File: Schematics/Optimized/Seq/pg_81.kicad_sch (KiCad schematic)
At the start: 23 parts, among them U8201 F04, U8203 8051, U8204 F04, U8205 F174, U8206 F245, U8207 F240, U8208 F174, U8209 F175, U8210 F194, U8211 F04, U8212 F30, U8213 F04, U8214 F00, U8215 F00, U8216 F38, U8217 F04, U8218 F02, U8219 F00, U8220 F00, U8221 F00, U8222 F00

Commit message: SEQ condensation
Tested: passed run_udiag
Tested: passed expmon_test_seq --quick
Tested: 16.7s (&c) boot_env
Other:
- moved on the sheet: GB244, U8201
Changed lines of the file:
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@@
     (comment 4 "RELEASED")
   )
-  (junction (at 45.72 20.32) (diameter 0) (color 0 0 0 0)
+  (junction (at 142.24 60.96) (diameter 0) (color 0 0 0 0)
   )
   (junction (at 281.94 73.66) (diameter 0) (color 0 0 0 0)
   )
+  (junction (at 208.28 73.66) (diameter 0) (color 0 0 0 0)
+  )
   (junction (at 408.94 243.84) (diameter 0) (color 0 0 0 0)
   )
@@
   )
   (junction (at 40.64 299.72) (diameter 0) (color 0 0 0 0)
-  )
-  (junction (at 213.36 73.66) (diameter 0) (color 0 0 0 0)
   )
   (no_connect (at 515.62 195.58))
@@
     (stroke (width 0) (type default))
   )
-  (wire (pts (xy 40.64 20.32) (xy 45.72 20.32))
+  (wire (pts (xy 137.16 60.96) (xy 142.24 60.96))
     (stroke (width 0) (type default))
   )
@@
     (stroke (width 0) (type default))
   )
-  (wire (pts (xy 96.52 20.32) (xy 213.36 20.32))
+  (wire (pts (xy 193.04 60.96) (xy 208.28 60.96))
     (stroke (width 0) (type default))
   )
@@
     (stroke (width 0) (type default))
   )
-  (wire (pts (xy 157.48 101.6) (xy 177.8 101.6))
+  (wire (pts (xy 172.72 101.6) (xy 177.8 101.6))
     (stroke (width 0) (type default))
   )
@@
     (stroke (width 0) (type default))
   )
-  (wire (pts (xy 175.26 76.2) (xy 190.5 76.2))
+  (wire (pts (xy 182.88 76.2) (xy 190.5 76.2))
     (stroke (width 0) (type default))
   )
@@
     (stroke (width 0) (type default))
   )
-  (wire (pts (xy 213.36 20.32) (xy 213.36 73.66))
+  (wire (pts (xy 208.28 60.96) (xy 208.28 73.66))
     (stroke (width 0) (type default))
   )
@@
     (stroke (width 0) (type default))
   )
+  (wire (pts (xy 208.28 73.66) (xy 236.22 73.66))
+    (stroke (width 0) (type default))
+  )
   (wire (pts (xy 548.64 180.34) (xy 551.18 180.34))
     (stroke (width 0) (type default))
@@
     (stroke (width 0) (type default))
   )
-  (wire (pts (xy 43.18 27.94) (xy 45.72 27.94))
+  (wire (pts (xy 139.7 68.58) (xy 142.24 68.58))
     (stroke (width 0) (type default))
   )
@@
     (stroke (width 0) (type default))
   )
-  (wire (pts (xy 45.72 20.32) (xy 76.2 20.32))
+  (wire (pts (xy 142.24 60.96) (xy 172.72 60.96))
     (stroke (width 0) (type default))
   )
@@
     (stroke (width 0) (type default))
   )
-  (wire (pts (xy 154.94 172.72) (xy 177.8 172.72))
+  (wire (pts (xy 172.72 172.72) (xy 177.8 172.72))
     (stroke (width 0) (type default))
   )
@@
     (stroke (width 0) (type default))
   )
-  (wire (pts (xy 45.72 27.94) (xy 45.72 20.32))
-    (stroke (width 0) (type default))
-  )
-  (wire (pts (xy 213.36 73.66) (xy 236.22 73.66))
+  (wire (pts (xy 142.24 68.58) (xy 142.24 60.96))
     (stroke (width 0) (type default))
   )
@@
     (stroke (width 0) (type default))
   )
-  (wire (pts (xy 142.24 203.2) (xy 177.8 203.2))
+  (wire (pts (xy 162.56 203.2) (xy 177.8 203.2))
     (stroke (width 0) (type default))
   )
@@
     (stroke (width 0) (type default))
   )
-  (wire (pts (xy 175.26 78.74) (xy 175.26 76.2))
+  (wire (pts (xy 182.88 78.74) (xy 182.88 76.2))
     (stroke (width 0) (type default))
   )
@@
     (stroke (width 0) (type default))
   )
-  (wire (pts (xy 215.9 246.38) (xy 241.3 246.38))
+  (wire (pts (xy 215.9 246.38) (xy 223.52 246.38))
     (stroke (width 0) (type default))
   )
@@
     (stroke (width 0) (type default))
   )
-  (wire (pts (xy 208.28 73.66) (xy 213.36 73.66))
-    (stroke (width 0) (type default))
-  )
   (wire (pts (xy 360.68 111.76) (xy 370.84 111.76))
     (stroke (width 0) (type default))
@@
     (effects (font (size 2.54 2.54)) (justify left bottom))
   )
-  (label "WR~" (at 152.4 203.2 0) (fields_autoplaced)
+  (label "WR~" (at 162.56 203.2 0) (fields_autoplaced)
     (effects (font (size 2.54 2.54)) (justify left bottom))
   )
@@
     )
   )
-  (global_label "Q.DIAG_FREEZE~" (shape bidirectional) (at 241.3 246.38 0) (fields_autoplaced)
+  (global_label "Q.DIAG_FREEZE~" (shape bidirectional) (at 223.52 246.38 0) (fields_autoplaced)
     (effects (font (size 2.54 2.54)) (justify left))
-    (property "Intersheetrefs" "${INTERSHEET_REFS}" (at 276.2431 246.2213 0)
+    (property "Intersheetrefs" "${INTERSHEET_REFS}" (at 258.4631 246.2213 0)
       (effects (font (size 1.905 1.905)) (justify left))
     )
@@
     )
   )
-  (global_label "CLK.2X" (shape input) (at 157.48 101.6 180) (fields_autoplaced)
-    (effects (font (size 2.54 2.54)) (justify right))
-    (property "Intersheetrefs" "${INTERSHEET_REFS}" (at 138.6129 101.6 0)
+  (global_label "CLK.2X" (shape input) (at 172.72 101.6 180) (fields_autoplaced)
+    (effects (font (size 2.54 2.54)) (justify right))
+    (property "Intersheetrefs" "${INTERSHEET_REFS}" (at 153.8529 101.6 0)
       (effects (font (size 1.27 1.27)) (justify right))
     )
@@
     )
   )
-  (global_label "FSM_DONE~" (shape input) (at 154.94 172.72 180) (fields_autoplaced)
-    (effects (font (size 2.54 2.54)) (justify right))
-    (property "Intersheetrefs" "${INTERSHEET_REFS}" (at 128.7054 172.5613 0)
+  (global_label "FSM_DONE~" (shape input) (at 172.72 172.72 180) (fields_autoplaced)
+    (effects (font (size 2.54 2.54)) (justify right))
+    (property "Intersheetrefs" "${INTERSHEET_REFS}" (at 146.4854 172.5613 0)
       (effects (font (size 1.905 1.905)) (justify right))
     )
@@
     )
   )
-  (global_label "Q.RESET~" (shape bidirectional) (at 40.64 20.32 180) (fields_autoplaced)
-    (effects (font (size 2.54 2.54)) (justify right))
-    (property "Intersheetrefs" "${INTERSHEET_REFS}" (at 18.6388 20.1613 0)
+  (global_label "Q.RESET~" (shape bidirectional) (at 137.16 60.96 180) (fields_autoplaced)
+    (effects (font (size 2.54 2.54)) (justify right))
+    (property "Intersheetrefs" "${INTERSHEET_REFS}" (at 115.1588 60.8013 0)
       (effects (font (size 1.905 1.905)) (justify right))
     )
@@
     )
   )
-  (symbol (lib_id "r1000:PD") (at 175.26 78.74 0) (unit 1)
+  (symbol (lib_id "r1000:PD") (at 182.88 78.74 0) (unit 1)
     (in_bom no) (on_board yes) (dnp no)
-    (property "Reference" "#PWR0102" (at 175.26 78.74 0)
-      (effects (font (size 1.27 1.27)) hide)
-    )
-    (property "Value" "PD" (at 175.26 78.74 0)
-      (effects (font (size 1.27 1.27)) hide)
-    )
-    (property "Footprint" "" (at 175.26 78.74 0)
-      (effects (font (size 1.27 1.27)) hide)
-    )
-    (property "Datasheet" "" (at 175.26 78.74 0)
+    (property "Reference" "#PWR0102" (at 182.88 78.74 0)
+      (effects (font (size 1.27 1.27)) hide)
+    )
+    (property "Value" "PD" (at 182.88 78.74 0)
+      (effects (font (size 1.27 1.27)) hide)
+    )
+    (property "Footprint" "" (at 182.88 78.74 0)
+      (effects (font (size 1.27 1.27)) hide)
+    )
+    (property "Datasheet" "" (at 182.88 78.74 0)
       (effects (font (size 1.27 1.27)) hide)
     )
@@
     )
   )
-  (symbol (lib_id "r1000:GB") (at 43.18 27.94 0) (mirror y) (unit 1)
+  (symbol (lib_id "r1000:GB") (at 139.7 68.58 0) (mirror y) (unit 1)
     (in_bom yes) (on_board yes) (dnp no)
-    (property "Reference" "GB244" (at 39.37 27.94 0)
-      (effects (font (size 2.54 2.54)) (justify left))
-    )
-    (property "Value" "GB" (at 43.18 27.94 0)
-      (effects (font (size 1.27 1.27)) hide)
-    )
-    (property "Footprint" "" (at 43.18 27.94 0)
-      (effects (font (size 1.27 1.27)) hide)
-    )
-    (property "Datasheet" "" (at 43.18 27.94 0)
+    (property "Reference" "GB244" (at 135.89 68.58 0)
+      (effects (font (size 2.54 2.54)) (justify left))
+    )
+    (property "Value" "GB" (at 139.7 68.58 0)
+      (effects (font (size 1.27 1.27)) hide)
+    )
+    (property "Footprint" "" (at 139.7 68.58 0)
+      (effects (font (size 1.27 1.27)) hide)
+    )
+    (property "Datasheet" "" (at 139.7 68.58 0)
       (effects (font (size 1.27 1.27)) hide)
     )
@@
     )
   )
-  (symbol (lib_id "r1000:F04") (at 86.36 20.32 0) (unit 1)
+  (symbol (lib_id "r1000:F04") (at 182.88 60.96 0) (unit 1)
     (in_bom yes) (on_board yes) (dnp no)
-    (property "Reference" "U8201" (at 86.36 20.32 0)
+    (property "Reference" "U8201" (at 182.88 60.96 0)
       (effects (font (size 1.27 1.27)))
     )
-    (property "Value" "F04" (at 87.63 25.4 0)
-      (effects (font (size 2.54 2.54)) (justify left))
-    )
-    (property "Footprint" "" (at 86.36 20.32 0)
-      (effects (font (size 1.27 1.27)) hide)
-    )
-    (property "Datasheet" "" (at 86.36 20.32 0)
-      (effects (font (size 1.27 1.27)) hide)
-    )
-    (property "Location" "N39" (at 73.66 25.4 0)
-      (effects (font (size 2.54 2.54)) (justify left))
-    )
-    (property "Name" "DINV0A" (at 86.36 15.24 0)
+    (property "Value" "F04" (at 184.15 66.04 0)
+      (effects (font (size 2.54 2.54)) (justify left))
+    )
+    (property "Footprint" "" (at 182.88 60.96 0)
+      (effects (font (size 1.27 1.27)) hide)
+    )
+    (property "Datasheet" "" (at 182.88 60.96 0)
+      (effects (font (size 1.27 1.27)) hide)
+    )
+    (property "Location" "N39" (at 170.18 66.04 0)
+      (effects (font (size 2.54 2.54)) (justify left))
+    )
+    (property "Name" "DINV0A" (at 182.88 55.88 0)
       (effects (font (size 2.54 2.54)) (justify bottom))
     )

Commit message: Merge SEQ changes
Tested: passed run_udiag
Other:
- moved on the sheet: GB217, GB244, U8201, U8203, U8204, U8205, U8206, U8207, U8208, U8209, U8210, U8211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

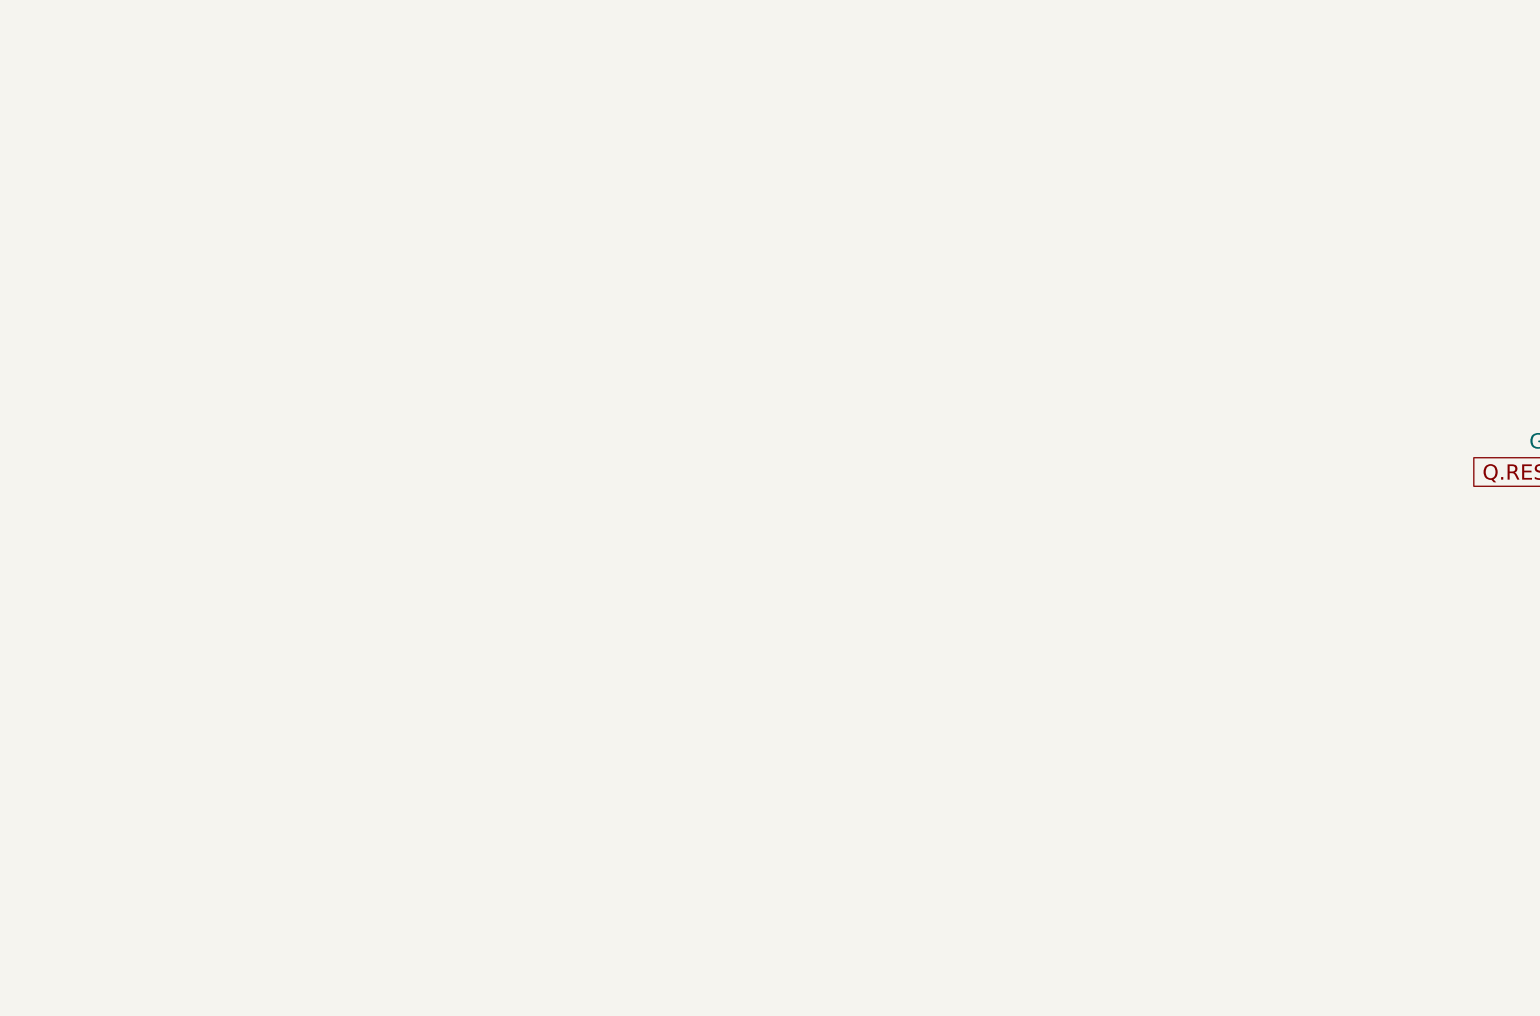
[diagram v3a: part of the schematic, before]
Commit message: IOC+SEQ improvements. (NB: contains IOC RTC de-racing)
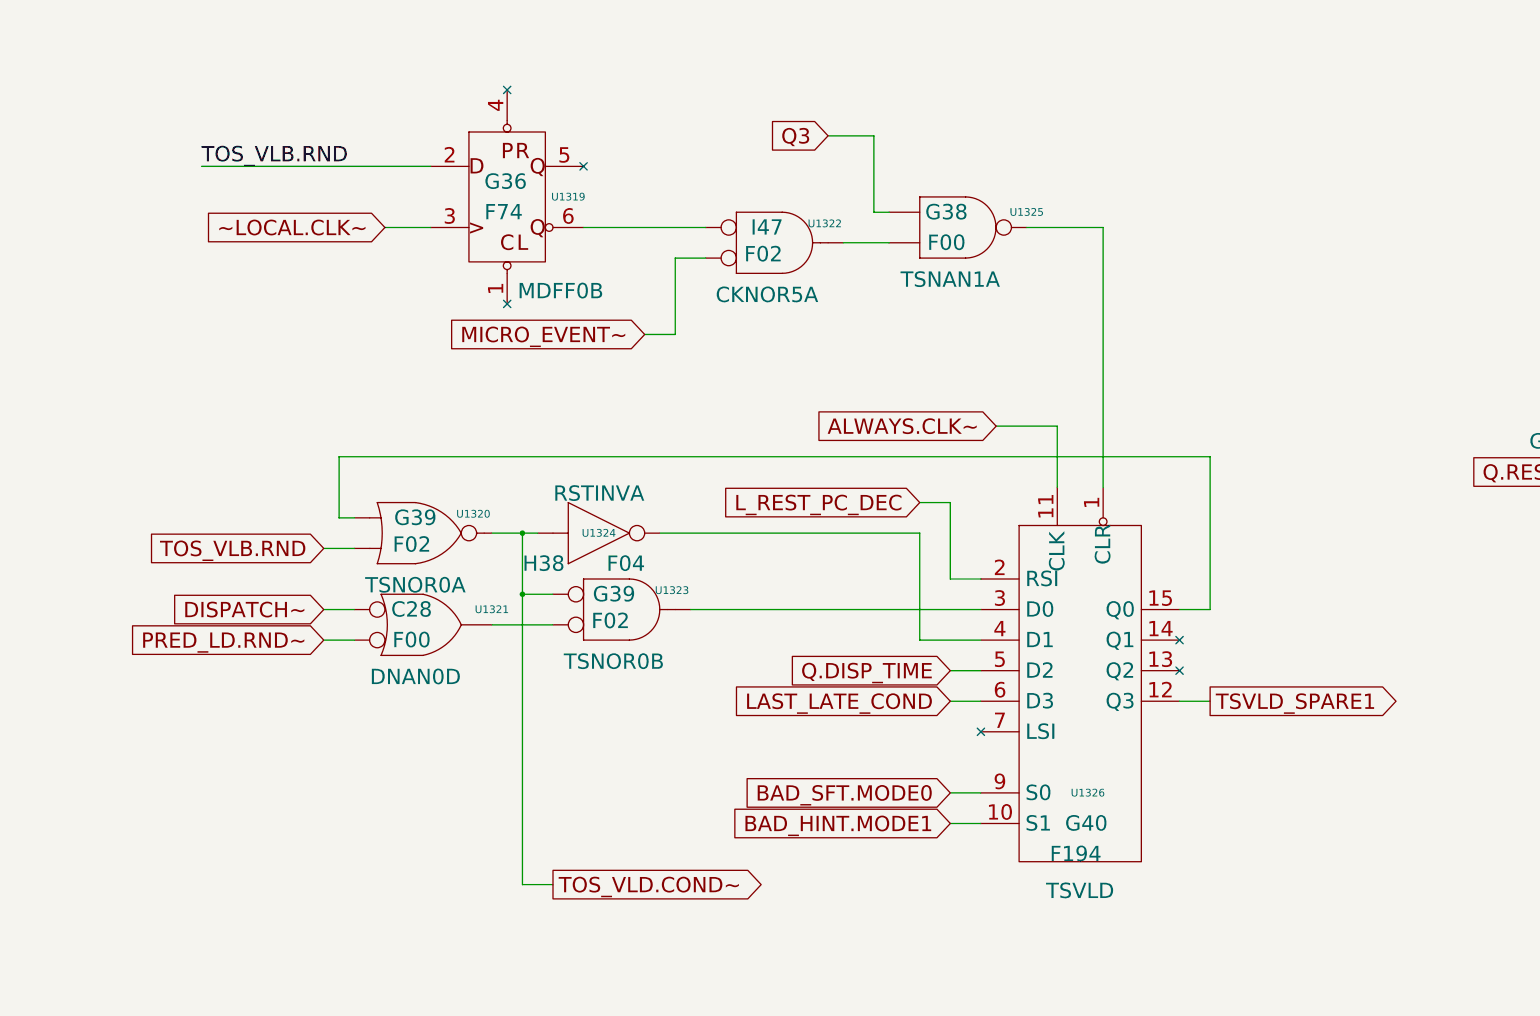
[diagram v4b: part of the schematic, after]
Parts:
- added U1319: F74, symbol r1000:F74
- added U1320, U1322, U1323: F02, symbol r1000:F02
- added U1321, U1325: F00, symbol r1000:F00
- added U1324: F04, symbol r1000:F04
- added U1326: F194, symbol r1000:F194
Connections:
- net ALWAYS.CLK~: now also U1326.11 (CLK)
- net TSVLD_SPARE1: now also U1326.12 (Q3)
- new net: U1325.3 (Q), U1326.1 (CLR)
- new net: U1320.1 (D0), U1326.15 (Q0)
- new net: U1323.3 (Q), U1326.3 (D0)
- new net: U1324.2 (Q), U1326.4 (D1)
- new net: U1321.3 (Q), U1323.2 (D1)
- new net: U1319.6 (Q_), U1322.1 (D0)
- new net: U1322.3 (Q), U1325.2 (D1)
- new net BAD_HINT.MODE1: U1326.10 (S1)
- new net BAD_SFT.MODE0: U1326.9 (S0)
- new net DISPATCH~: U1321.1 (D0)
- new net LAST_LATE_COND: U1326.6 (D3)
- new net L_REST_PC_DEC: U1326.2 (RSI)
- new net MICRO_EVENT~: U1322.2 (D1)
- new net PRED_LD.RND~: U1321.2 (D1)
- new net Q.DISP_TIME: U1326.5 (D2)
- new net Q3: U1325.1 (D0)
- new net TOS_VLB.RND: U1319.2 (D), U1320.2 (D1)
- new net TOS_VLD.COND~: U1320.3 (Q), U1323.1 (D0), U1324.1 (D0)
- new net ~LOCAL.CLK~: U1319.3 (CLK)
- no-connect marks 27 -> 33

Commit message: SEQ condensation
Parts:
- removed U8206: F245, symbol r1000:F245
- renumbered U1320 to U2604, U1321 to U2605, U1319 to U2606, U1324 to U2607, U1323 to U2608, U1322 to U2609, U1325 to U2610, U1326 to U2611
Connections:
- net DP0 is gone; now on net DIAG.D0: U8203.8 (B0)
- net DP1 is gone; now on net DIAG.D1: U8203.7 (B1)
- net DP2 is gone; now on net DIAG.D2: U8203.6 (B2)
- net DP3 is gone; now on net DIAG.D3: U8203.5 (B3)
- net DP4 is gone; now on net DIAG.D4: U8203.4 (B4)
- net DP5 is gone; now on net DIAG.D5: U8203.3 (B5)
- net DP6 is gone; now on net DIAG.D6: U8203.2 (B6)
- net DP7 is gone; now on net DIAG.D7: U8203.1 (B7)
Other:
- moved on the sheet: U8205, U8207, U8208, U8210

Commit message: Much work in SEQ and MEM32
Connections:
- net DFREEZE.FSM~: now also U8212.11 (D0); no longer U8212.5 (D6)
- net DIAG.CMD5: now also U8208.2 (Q0); no longer U8208.10 (Q3)
- net DIAG.CMD6: now also U8208.5 (Q1); no longer U8208.12 (Q4)
- net DIAG.CMD7: now also U8208.7 (Q2); no longer U8208.15 (Q5)
- net HALT~: now also U8212.2 (D3); no longer U8212.3 (D4)
- net PERR0~: now also U8212.3 (D4); no longer U8212.11 (D0)
- net PERR1~: now also U8212.4 (D5); no longer U8212.12 (D1)
- net PERR2~: now also U8212.5 (D6); no longer U8212.1 (D2)
- net PERR3~: now also U8212.6 (D7); no longer U8212.2 (D3)
- net PERR4~: now also U8212.12 (D1); no longer U8212.4 (D5)
- net SYNC_FREZ.EN: now also U8216.1 (D0); no longer U8216.2 (D1)
- net TBUS.PERR~: now also U8221.3 (Q); no longer U8220.3 (Q)
- net TYP_PERR.MCHK: now also U8221.2 (D1); no longer U8220.1 (D0)
- net VAL_PERR.MCHK: now also U8220.1 (D0); no longer U8221.2 (D1)
- net VBUS.PERR~: now also U8220.3 (Q); no longer U8221.3 (Q)
- net at U8203.37 (A5): now also U8208.3 (D0); no longer U8208.11 (D3)
- net at U8203.38 (A6): now also U8208.4 (D1); no longer U8208.13 (D4)
- net at U8203.39 (A7): now also U8208.6 (D2); no longer U8208.14 (D5)
- net at U8215.3 (Q): now also U8216.2 (D1); no longer U8216.1 (D0)
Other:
- moved on the sheet: GB217, GB244, U2604, U2605, U2606, U2607, U2608, U2609, U2610, U2611, U8201, U8203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
